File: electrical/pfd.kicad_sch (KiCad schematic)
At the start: 12 parts

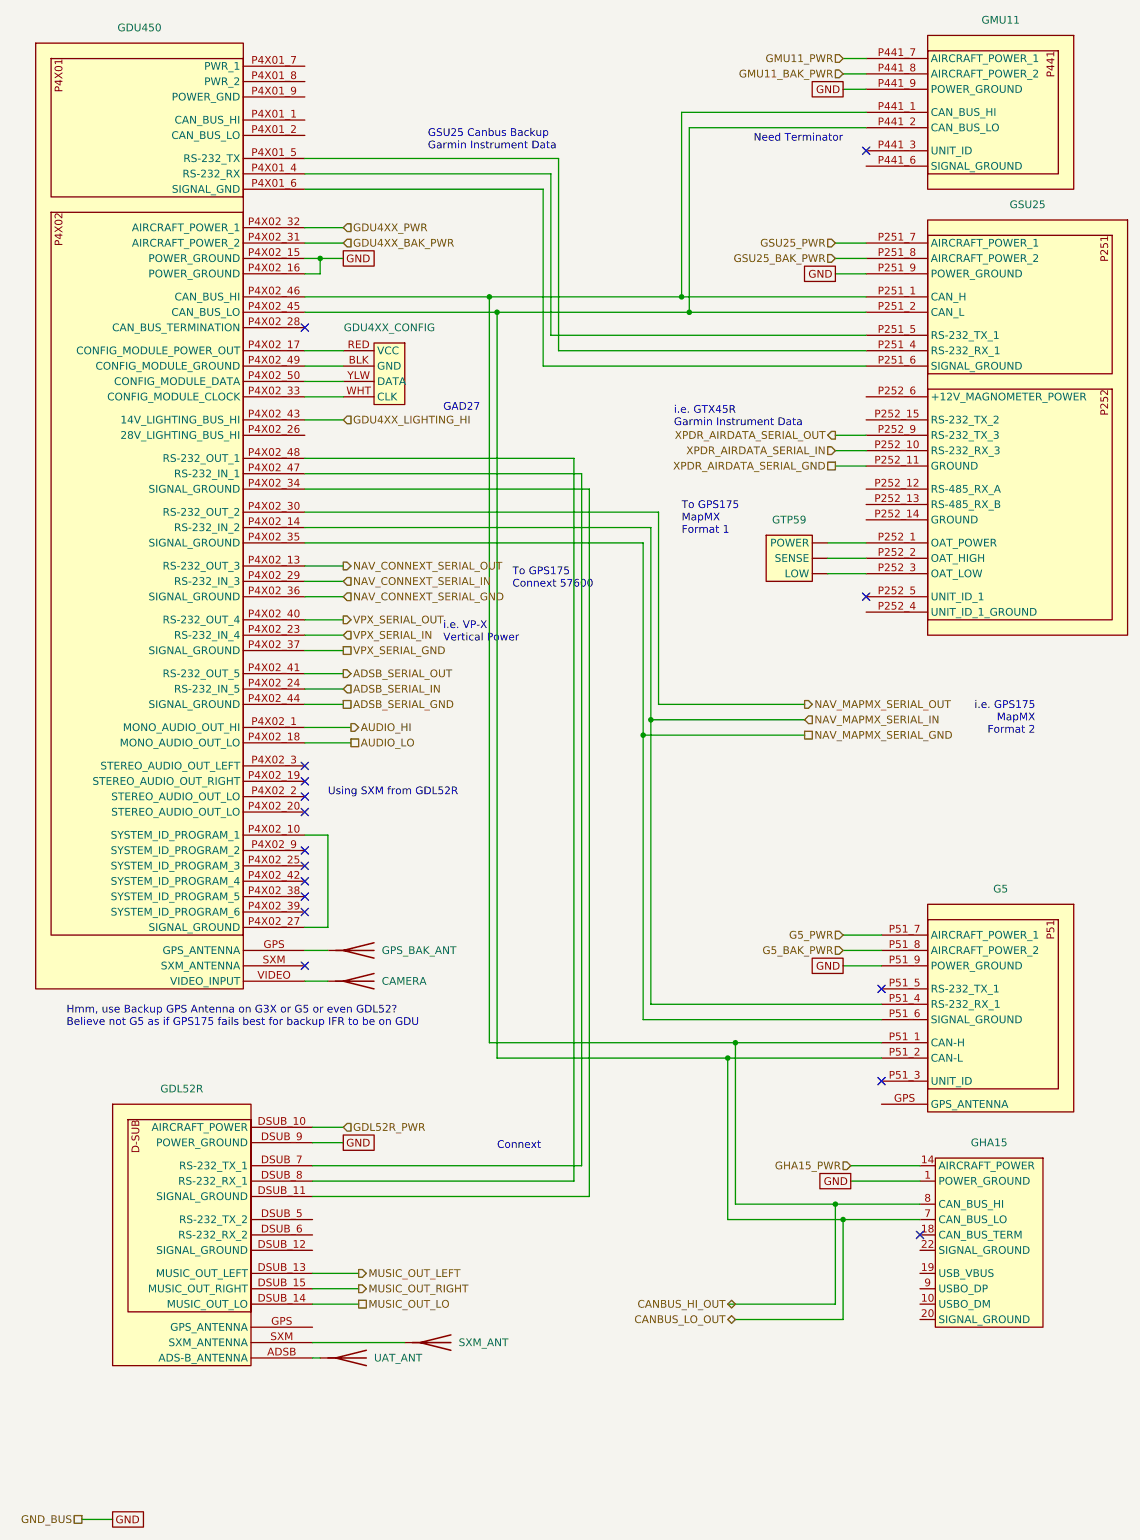
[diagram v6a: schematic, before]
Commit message: Updated settings for RS-232, etc.
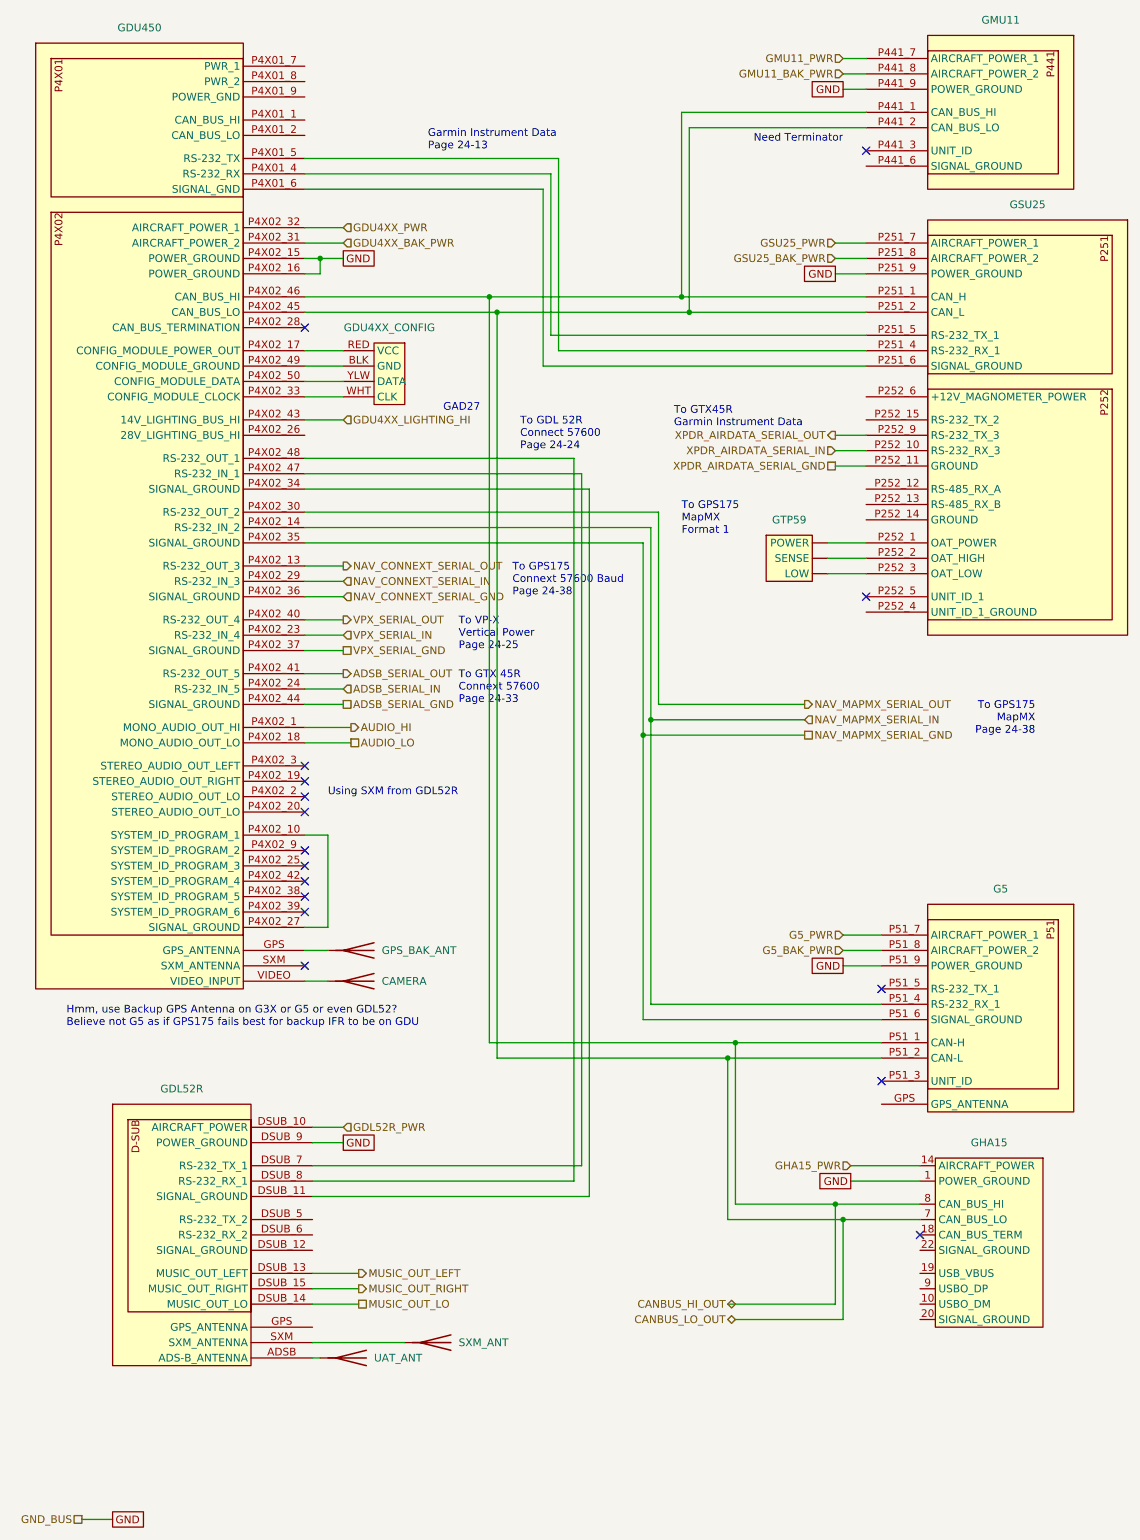
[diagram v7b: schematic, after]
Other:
- note added: "Garmin Instrument Data Page 24-13"
- note added: "To GDL 52R Connect 57600 Page 24-24"
- note added: "To GPS175 Connext 57600 Baud Page 24-38"
- note added: "To GPS175 MapMX Page 24-38"
- note added: "To GTX 45R Connext 57600 Page 24-33"
- note added: "To GTX45R Garmin Instrument Data"
- note added: "To VP-X Vertical Power Page 24-25"
- note removed: "Connext"
- note removed: "GSU25 Canbus Backup Garmin Instrument Data"
- note removed: "To GPS175 Connext 57600"
- note removed: "i.e. GPS175 MapMX Format 2"
- note removed: "i.e. GTX45R Garmin Instrument Data"
- note removed: "i.e. VP-X Vertical Power"
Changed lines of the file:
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@@
     (stroke (width 0) (type default))
   )
-  (text "i.e. VP-X\nVertical Power" (at 85.09 116.84 0)
+  (text "To VP-X\nVertical Power\nPage 24-25" (at 87.63 118.11 0)
     (effects (font (size 1.27 1.27)) (justify left bottom))
   )
@@
     (effects (font (size 1.27 1.27)) (justify left bottom))
   )
-  (text "Connext" (at 93.98 200.66 0)
+  (text "To GPS175\nMapMX\nPage 24-38" (at 182.88 132.08 0)
+    (effects (font (size 1.27 1.27)) (justify right bottom))
+  )
+  (text "To GTX 45R\nConnext 57600\nPage 24-33" (at 87.63 127 0)
     (effects (font (size 1.27 1.27)) (justify left bottom))
   )
-  (text "i.e. GPS175\nMapMX\nFormat 2" (at 182.88 132.08 0)
-    (effects (font (size 1.27 1.27)) (justify right bottom))
-  )
-  (text "i.e. GTX45R\nGarmin Instrument Data" (at 123.19 81.28 0)
+  (text "To GTX45R\nGarmin Instrument Data" (at 123.19 81.28 0)
     (effects (font (size 1.27 1.27)) (justify left bottom))
   )
@@
     (effects (font (size 1.27 1.27)) (justify left bottom))
   )
-  (text "GSU25 Canbus Backup\nGarmin Instrument Data" (at 82.55 35.56 0)
+  (text "Garmin Instrument Data\nPage 24-13" (at 82.55 35.56 0)
+    (effects (font (size 1.27 1.27)) (justify left bottom))
+  )
+  (text "To GDL 52R\nConnect 57600\nPage 24-24" (at 97.79 85.09 0)
     (effects (font (size 1.27 1.27)) (justify left bottom))
   )
@@
     (effects (font (size 1.27 1.27)) (justify left bottom))
   )
-  (text "To GPS175\nConnext 57600" (at 96.52 107.95 0)
+  (text "To GPS175\nConnext 57600 Baud\nPage 24-38" (at 96.52 109.22 0)
     (effects (font (size 1.27 1.27)) (justify left bottom))
   )

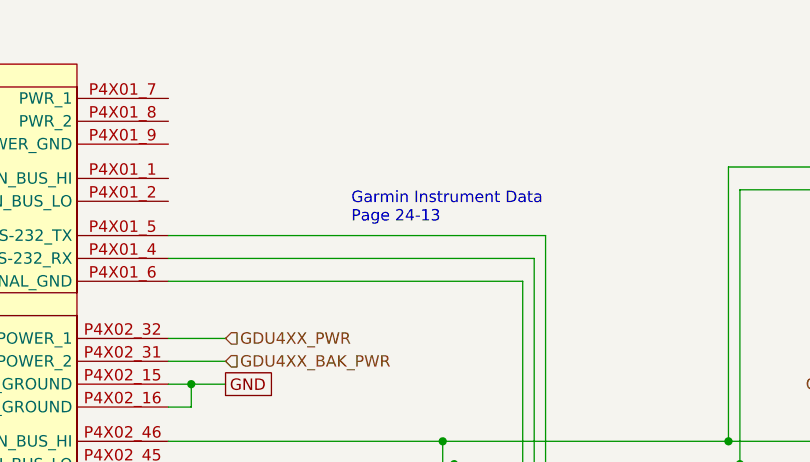
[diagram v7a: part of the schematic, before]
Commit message: Removed Amps as Rotax sends that over Can to GEA24
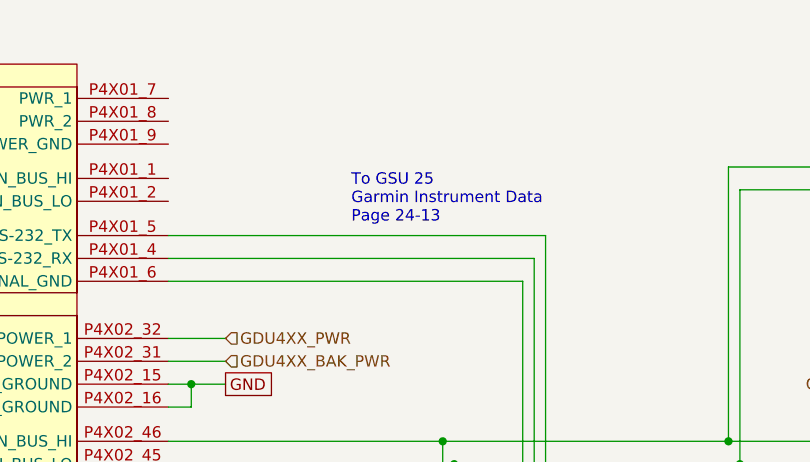
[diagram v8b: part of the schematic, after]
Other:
- note added: "To GSU 25 Garmin Instrument Data Page 24-13"
- note removed: "Garmin Instrument Data Page 24-13"
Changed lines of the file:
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@@
     (effects (font (size 1.27 1.27)) (justify left bottom))
   )
-  (text "Garmin Instrument Data\nPage 24-13" (at 82.55 35.56 0)
+  (text "To GSU 25\nGarmin Instrument Data\nPage 24-13" (at 82.55 35.56 0)
     (effects (font (size 1.27 1.27)) (justify left bottom))
   )
